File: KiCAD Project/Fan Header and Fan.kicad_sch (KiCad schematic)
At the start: 7 parts, among them J2 B2B-XH-A(LF)(SN), J3 ESW-120-33-G-D, M1 CFM-2507CF-050-089, U7 CAT24C32HU4I-GT3

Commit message: v1.0.0 RC2
Build candidate 2
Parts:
- J2: Mouser Part Number (none) -> 306-B2BXHALFSNP; Mouser Price/Stock (none) -> https://www.mouser.com/ProductDetail/JST-Commercial/B2B-XH-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; Spec (none) -> JST-XH-2
- M1: value CFM-2507CF-050-089 -> CFM-2510B-070-140; footprint DW_Mechanical:[Fan] SameSky CFM-2507CF-050-089 -> DW_Mechanical:[Fan] SameSky CFM-2510B-070-140; symbol DW_Mechanical:[Fan] SameSky CFM-2507CF-050-089 -> DW_Mechanical:[Fan] SameSky CFM-2510B-070-140; Height 7 -> 10; Manufacturer_Part_Number CFM-2507CF-050-089 -> CFM-2510B-070-140; Mouser Part Number 179-CFM2507CF050089 -> 490-CFM2510B-070-140; Mouser Price/Stock https://www.mouser.com/ProductDetail/Same-Sky/CFM-2507CF-05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 -> https://www.mouser.com/ProductDetail/Same-Sky/CFM-2510B-070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; Spec (none) -> 5V 7000RPM 25mm
- U7: Spec (none) -> CAT24C32HU4I-GT3
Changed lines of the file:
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@@
 			)
 		)
-		(property "Spec" ""
+		(property "Spec" "CAT24C32HU4I-GT3"
 			(at 96.52 101.6 0)
 			(effects
@@
 		(on_board yes)
 		(dnp no)
-		(fields_autoplaced yes)
 		(property "Reference" "J2"
 			(at 155.702 50.8578 0)
@@
 			)
 		)
-		(property "Mouser Part Number" ""
+		(property "Mouser Part Number" "306-B2BXHALFSNP"
 			(at 147.32 53.34 0)
 			(effects
@@
 				)
 				(hide yes)
+			)
+		)
+		(property "Spec" "JST-XH-2"
+			(at 160.655 55.245 0)
+			(effects
+				(font
+					(size 1.27 1.27)
+				)
+			)
+		)
+		(property "Mouser Price/Stock" "https://www.mouser.com/ProductDetail/JST-Commercial/B2B-XH-ALFSN?qs=cdbOS8ANM9DdcSn9qRmfCw%3D%3D"
+			(at 147.32 53.34 0)
+			(effects
+				(font
+					(size 1.27 1.27)
+				)
 			)
 		)
@@
 	)
 	(symbol
-		(lib_id "DW_Mechanical:[Fan] SameSky CFM-2507CF-050-089")
+		(lib_id "DW_Mechanical:[Fan] SameSky CFM-2510B-070-140")
 		(at 209.55 50.8 0)
 		(unit 1)
@@
 			)
 		)
-		(property "Value" "CFM-2507CF-050-089"
+		(property "Value" "CFM-2510B-070-140"
 			(at 219.0749 52.0121 0)
 			(effects
@@
 			)
 		)
-		(property "Footprint" "DW_Mechanical:[Fan] SameSky CFM-2507CF-050-089"
+		(property "Footprint" "DW_Mechanical:[Fan] SameSky CFM-2510B-070-140"
 			(at 209.55 80.01 0)
 			(effects
@@
 			)
 		)
-		(property "Datasheet" "https://www.sameskydevices.com/product/resource/cfm-25cf.pdf"
+		(property "Datasheet" "https://www.sameskydevices.com/product/resource/cfm-25b.pdf"
 			(at 209.55 62.23 0)
 			(effects
@@
 			)
 		)
-		(property "Description" "DC Fans dc axial fan, 25 mm square, 7 mm, 5 Vdc, omniCOOL, 5000 RPM, 1.10 CFM"
+		(property "Description" "DC Fans dc axial fan, 25 mm square, 10 mm, 5 Vdc, omniCOOL, 5000 RPM, 1.35 CFM"
 			(at 209.55 74.93 0)
 			(effects
@@
 			)
 		)
-		(property "Height" "7"
+		(property "Height" "10"
 			(at 209.55 64.77 0)
 			(effects
@@
 			)
 		)
-		(property "Manufacturer_Part_Number" "CFM-2507CF-050-089"
+		(property "Manufacturer_Part_Number" "CFM-2510B-070-140"
 			(at 209.55 77.47 0)
 			(effects
@@
 			)
 		)
-		(property "Mouser Part Number" "179-CFM2507CF050089"
+		(property "Mouser Part Number" "490-CFM2510B-070-140"
 			(at 209.55 72.39 0)
 			(effects
@@
 			)
 		)
-		(property "Mouser Price/Stock" "https://www.mouser.com/ProductDetail/Same-Sky/CFM-2507CF-050-089?qs=ulEaXIWI0c9ptEGd6uhKEA%3D%3D"
+		(property "Mouser Price/Stock" "https://www.mouser.com/ProductDetail/Same-Sky/CFM-2510B-070-140?qs=GedFDFLaBXHD1VXBjs5CMA%3D%3D"
 			(at 209.55 69.85 0)
 			(effects
@@
 			)
 		)
+		(property "Spec" "5V 7000RPM 25mm"
+			(at 209.55 50.8 0)
+			(effects
+				(font
+					(size 1.27 1.27)
+				)
+			)
+		)

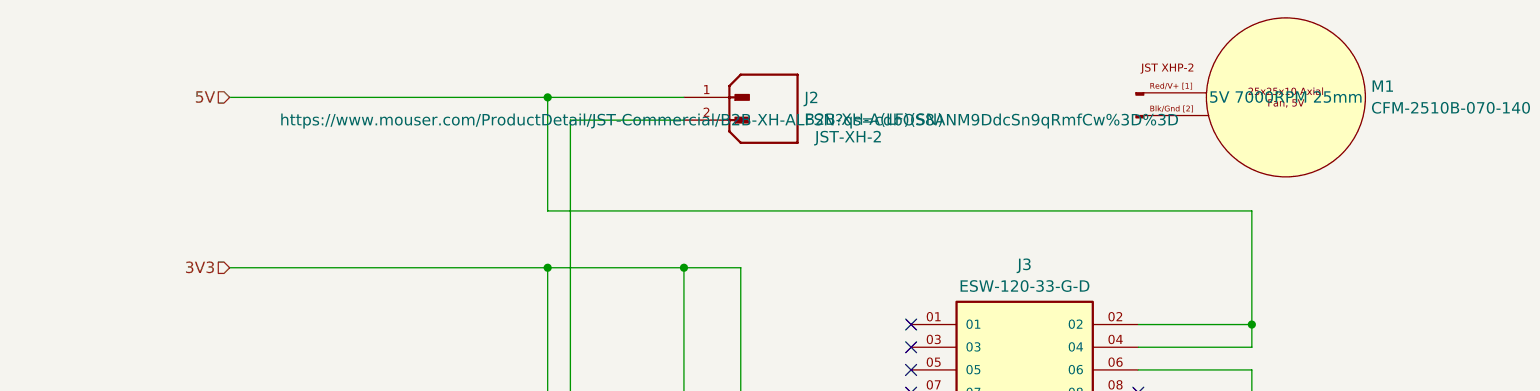
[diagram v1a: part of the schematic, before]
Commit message: v1.0.0 RC3
Minor change to upstream USB port to connect Vbus to ESD protection vice on-board 5V.
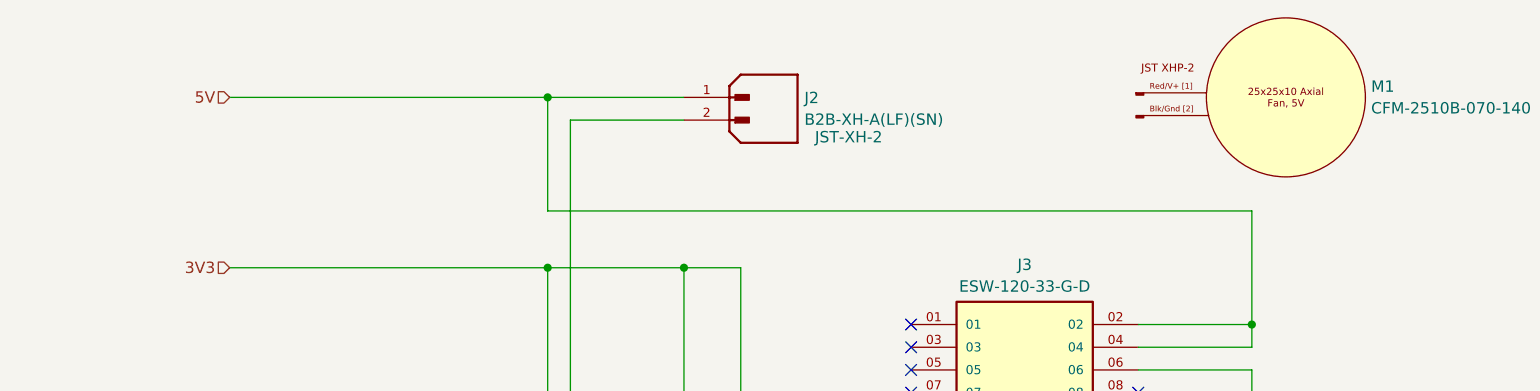
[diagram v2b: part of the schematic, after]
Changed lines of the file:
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@@
 		(title "1026 RPi Power Hat")
 		(date "2025-04-11")
-		(rev "1")
+		(rev "1.0.0 RC3")
 		(company "Dan Wilson")
 		(comment 1 "Copyright © 2025 Dan Wilson")
@@
 					(size 1.27 1.27)
 				)
+				(hide yes)
 			)
 		)
@@
 					(size 1.27 1.27)
 				)
-			)
-		)
+				(hide yes)
+			)
+		)

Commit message: v1.0.0A
Moved all symbols, footprints, and 3D models to local project-specific libraries in /KiCAD Project/Libraries.
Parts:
- C52: footprint Capacitor_SMD:C_0402_1005Metric -> 1026-3D:C_0402_1005Metric; symbol Device:C -> 1026-3D:C
- J2: footprint DW_Connectors:JST_B2B-XH-A(LF)(SN) -> 1026-3D:JST_B2B-XH-A(LF)(SN); symbol DW_Connectors:[J] JST B2B-XH-A(LF)(SN) -> 1026-3D:[J] JST B2B-XH-A(LF)(SN)
- J3: footprint DW_Connectors:[J] Samtec Elevated Socket Strip ESW-120-33-G-D -> 1026-3D:[J] Samtec Elevated Socket Strip ESW-120-33-G-D; symbol DW_Connectors:[J] Samtec ESW-120-33-G-D -> 1026-3D:[J] Samtec ESW-120-33-G-D
- M1: footprint DW_Mechanical:[Fan] SameSky CFM-2510B-070-140 -> 1026-3D:[Fan] SameSky CFM-2510B-070-140; symbol DW_Mechanical:[Fan] SameSky CFM-2510B-070-140 -> 1026-3D:[Fan] SameSky CFM-2510B-070-140
- R34, R35: footprint Resistor_SMD:R_0402_1005Metric -> 1026-3D:R_0402_1005Metric; symbol Device:R_US -> 1026-3D:R_US
- U7: footprint DW_Semiconductors:[U] OnSemi Serial EEPROM 4KB CAT24C32HU4I-GT3 -> 1026-3D:[U] OnSemi Serial EEPROM 4KB CAT24C32HU4I-GT3; symbol DW_Semiconductors:[U] OnSemi Serial EEPROM 4KB CAT24C32HU4I-GT3 -> 1026-3D:[U] OnSemi Serial EEPROM 4KB CAT24C32HU4I-GT3
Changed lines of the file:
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@@
 	)
 	(symbol
-		(lib_id "DW_Semiconductors:[U] OnSemi Serial EEPROM 4KB CAT24C32HU4I-GT3")
+		(lib_id "1026-3D:[U] OnSemi Serial EEPROM 4KB CAT24C32HU4I-GT3")
 		(at 96.52 101.6 0)
 		(unit 1)
@@
 			)
 		)
-		(property "Footprint" "DW_Semiconductors:[U] OnSemi Serial EEPROM 4KB CAT24C32HU4I-GT3"
+		(property "Footprint" "1026-3D:[U] OnSemi Serial EEPROM 4KB CAT24C32HU4I-GT3"
 			(at 118.11 196.52 0)
 			(effects
@@
 	)
 	(symbol
-		(lib_id "Device:R_US")
+		(lib_id "1026-3D:R_US")
 		(at 142.24 93.98 180)
 		(unit 1)
@@
 			)
 		)
-		(property "Footprint" "Resistor_SMD:R_0402_1005Metric"
+		(property "Footprint" "1026-3D:R_0402_1005Metric"
 			(at 141.224 93.726 90)
 			(effects
@@
 	)
 	(symbol
-		(lib_id "Device:R_US")
+		(lib_id "1026-3D:R_US")
 		(at 148.59 93.98 180)
 		(unit 1)
@@
 			)
 		)
-		(property "Footprint" "Resistor_SMD:R_0402_1005Metric"
+		(property "Footprint" "1026-3D:R_0402_1005Metric"
 			(at 147.574 93.726 90)
 			(effects
@@
 	)
 	(symbol
-		(lib_id "DW_Connectors:[J] JST B2B-XH-A(LF)(SN)")
+		(lib_id "1026-3D:[J] JST B2B-XH-A(LF)(SN)")
 		(at 147.32 53.34 0)
 		(unit 1)
@@
 			)
 		)
-		(property "Footprint" "DW_Connectors:JST_B2B-XH-A(LF)(SN)"
+		(property "Footprint" "1026-3D:JST_B2B-XH-A(LF)(SN)"
 			(at 147.32 64.77 0)
 			(effects
@@
 	)
 	(symbol
-		(lib_id "power:GND")
+		(lib_id "1026-3D:GND")
 		(at 66.04 139.7 0)
 		(unit 1)
@@
 	)
 	(symbol
-		(lib_id "DW_Connectors:[J] Samtec ESW-120-33-G-D")
+		(lib_id "1026-3D:[J] Samtec ESW-120-33-G-D")
 		(at 180.34 101.6 0)
 		(unit 1)
@@
 			)
 		)
-		(property "Footprint" "DW_Connectors:[J] Samtec Elevated Socket Strip ESW-120-33-G-D"
+		(property "Footprint" "1026-3D:[J] Samtec Elevated Socket Strip ESW-120-33-G-D"
 			(at 180.34 151.13 0)
 			(effects
@@
 	)
 	(symbol
-		(lib_id "Device:C")
+		(lib_id "1026-3D:C")
 		(at 66.04 105.41 180)
 		(unit 1)
@@
 			)
 		)
-		(property "Footprint" "Capacitor_SMD:C_0402_1005Metric"
+		(property "Footprint" "1026-3D:C_0402_1005Metric"
 			(at 65.0748 101.6 0)
 			(effects
@@
 	)
 	(symbol
-		(lib_id "DW_Mechanical:[Fan] SameSky CFM-2510B-070-140")
+		(lib_id "1026-3D:[Fan] SameSky CFM-2510B-070-140")
 		(at 209.55 50.8 0)
 		(unit 1)
@@
 			)
 		)
-		(property "Footprint" "DW_Mechanical:[Fan] SameSky CFM-2510B-070-140"
+		(property "Footprint" "1026-3D:[Fan] SameSky CFM-2510B-070-140"
 			(at 209.55 80.01 0)
 			(effects

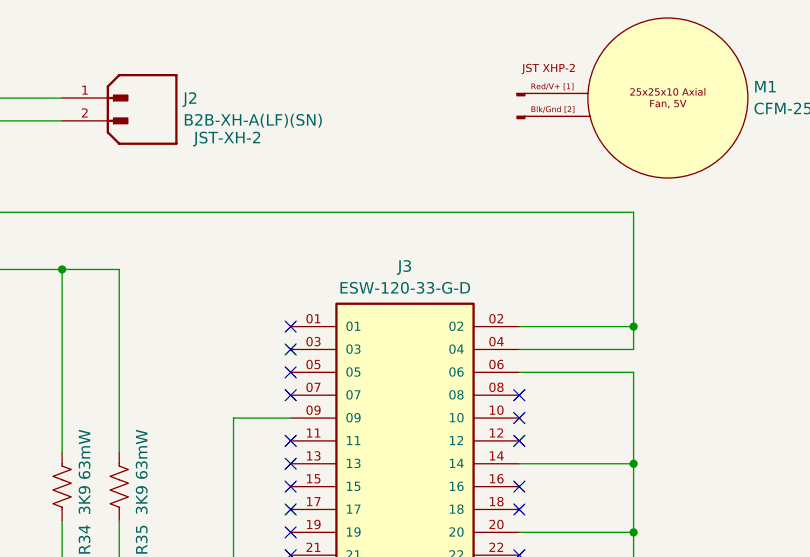
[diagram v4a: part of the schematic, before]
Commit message: New BOM for new Parts
Add ESW-120-34-G-D and remove ESW-120-33-G-D.  Update BOM and iBOM.
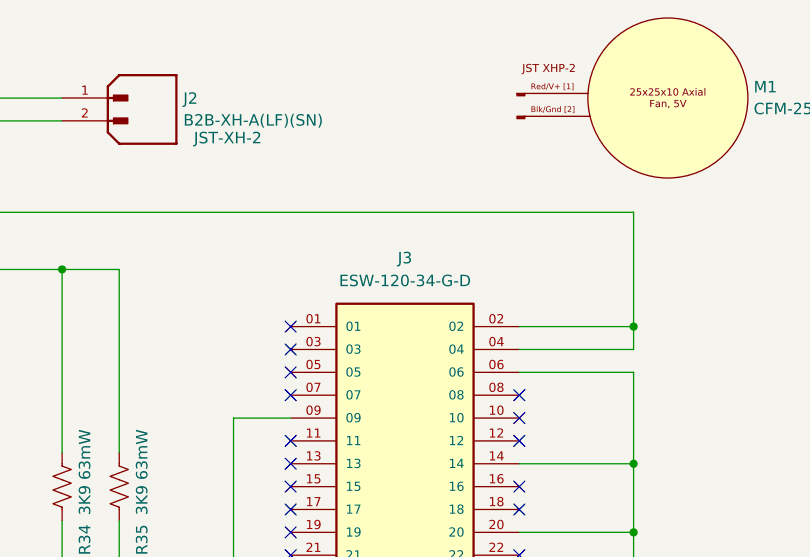
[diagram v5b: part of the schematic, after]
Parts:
- J3: value ESW-120-33-G-D -> ESW-120-34-G-D; footprint 1026-3D:[J] Samtec Elevated Socket Strip ESW-120-33-G-D -> 1026-3D:[J] Samtec Elevated Socket Strip ESW-120-34-G-D; symbol 1026-3D:[J] Samtec ESW-120-33-G-D -> 1026-3D:[J] Samtec ESW-120-34-G-D; Manufacturer_Part_Number ESW-120-33-G-D -> ESW-120-34-G-D; Mouser Part Number 200-ESW12033GD -> 200-ESW12034GD; Mouser Price/Stock https://www.mouser.com/ProductDetail/Samtec/ESW-120-33-G-D?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 -> https://www.mouser.com/ProductDetail/Samtec/ESW-120-34-G-D?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; Spec 20x2 0.1" Header -> 20x2 0.28" Header
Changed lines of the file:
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@@
 	)
 	(symbol
-		(lib_id "1026-3D:[J] Samtec ESW-120-33-G-D")
+		(lib_id "1026-3D:[J] Samtec ESW-120-34-G-D")
 		(at 180.34 101.6 0)
 		(unit 1)
@@
 		(fields_autoplaced yes)
 		(property "Reference" "J3"
-			(at 180.34 69.5155 0)
+			(at 180.34 68.58 0)
 			(effects
 				(font
@@
 			)
 		)
-		(property "Value" "ESW-120-33-G-D"
-			(at 180.34 71.9398 0)
+		(property "Value" "ESW-120-34-G-D"
+			(at 180.34 71.12 0)
 			(effects
 				(font
@@
 			)
 		)
-		(property "Footprint" "1026-3D:[J] Samtec Elevated Socket Strip ESW-120-33-G-D"
-			(at 180.34 151.13 0)
+		(property "Footprint" "1026-3D:[J] Samtec Elevated Socket Strip ESW-120-34-G-D"
+			(at 181.102 132.842 0)
 			(effects
 				(font
@@
 		)
 		(property "Datasheet" "https://www.mouser.com/datasheet/2/527/esw_th-2854089.pdf"
-			(at 180.34 132.08 0)
+			(at 181.864 129.794 0)
 			(effects
 				(font
@@
 			)
 		)
-		(property "Description" "Elevated Socket Strip 0.1in 20x2 16.13mmH Gold"
-			(at 180.34 134.62 0)
+		(property "Description" "Elevated Socket Strip 0.28in 20x2 16.13mmH Gold"
+			(at 182.372 134.366 0)
 			(effects
 				(font
@@
 		)
 		(property "Height" "16.13"
-			(at 180.34 142.24 0)
+			(at 180.34 101.6 0)
 			(effects
 				(font
@@
 		)
 		(property "Manufacturer_Name" "Samtec"
-			(at 180.34 147.32 0)
+			(at 180.34 101.6 0)
 			(effects
 				(font
@@
 			)
 		)
-		(property "Manufacturer_Part_Number" "ESW-120-33-G-D"
-			(at 180.34 139.7 0)
+		(property "Manufacturer_Part_Number" "ESW-120-34-G-D"
+			(at 180.34 101.6 0)
 			(effects
 				(font
@@
 			)
 		)
-		(property "Mouser Part Number" "200-ESW12033GD"
-			(at 180.34 137.16 0)
+		(property "Mouser Part Number" "200-ESW12034GD"
+			(at 180.34 101.6 0)
 			(effects
 				(font
@@
 			)
 		)
-		(property "Mouser Price/Stock" "https://www.mouser.com/ProductDetail/Samtec/ESW-120-33-G-D?qs=0lQeLiL1qybGjRGIrteP4Q%3D%3D"
-			(at 180.34 129.54 0)
+		(property "Mouser Price/Stock" "https://www.mouser.com/ProductDetail/Samtec/ESW-120-34-G-D?qs=0lQeLiL1qyZhSkNUS%2FXSIA%3D%3D"
+			(at 180.34 101.6 0)
 			(effects
 				(font
@@
 			)
 		)
-		(property "Spec" "20x2 0.1\" Header"
-			(at 180.34 144.78 0)
+		(property "Spec" "20x2 0.28\" Header"
+			(at 180.34 101.6 0)
 			(effects
 				(font
